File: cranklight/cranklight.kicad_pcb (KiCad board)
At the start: 2 copper layers, 80 x 35 mm, 24 parts, among them J1 Battery, J2 Bulb socket, Q1 Q_NMOS_GDS, SW1 SW_4PDT, U1 WeMos_mini, U2 PTN04050CAD

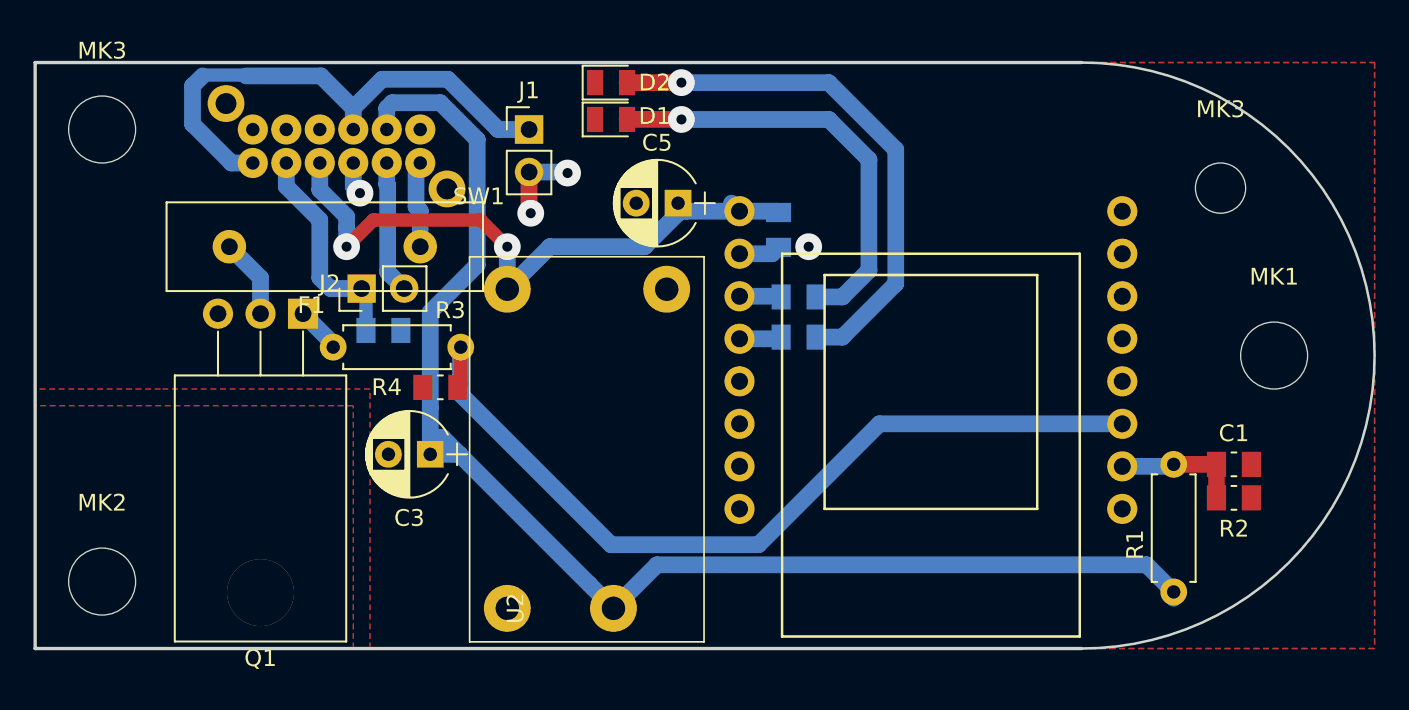
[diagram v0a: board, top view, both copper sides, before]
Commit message: Add fixes: move PTC, add charging connector, use switch as a simple switch
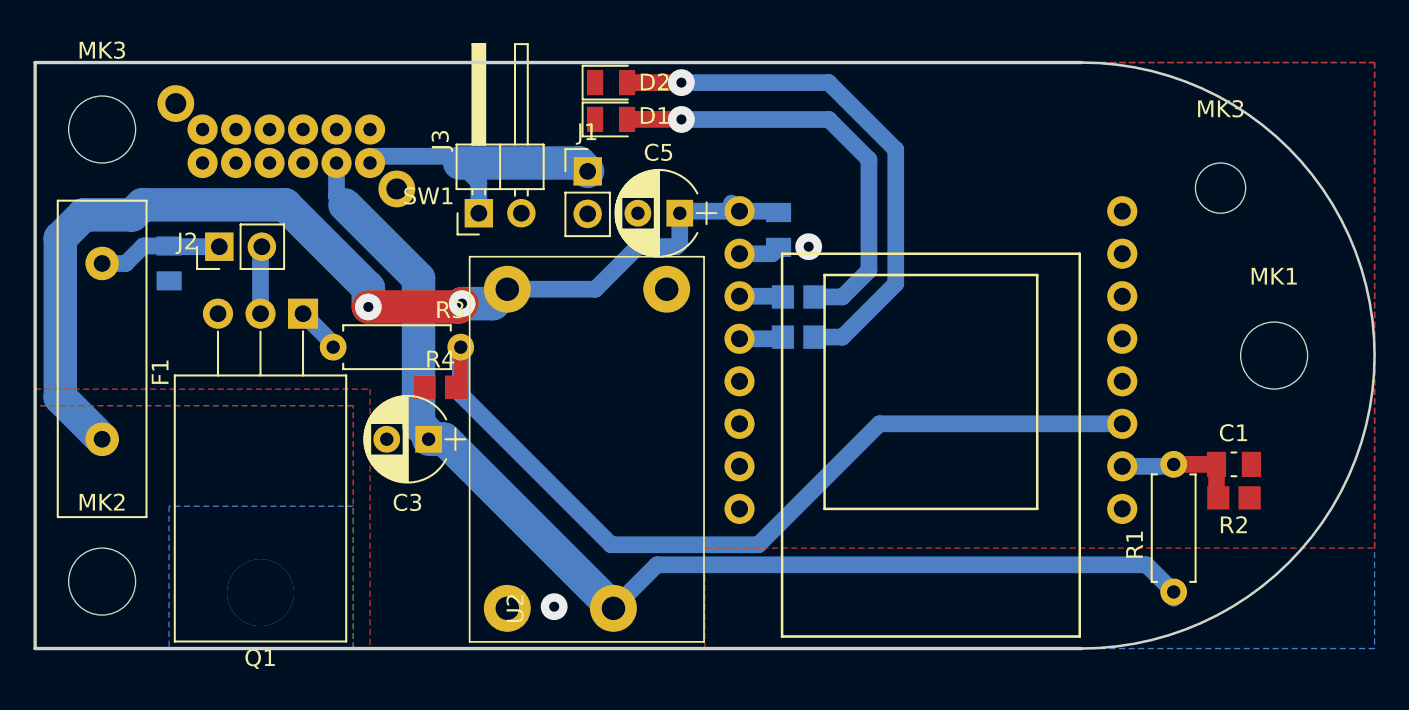
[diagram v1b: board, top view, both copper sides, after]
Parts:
- added J3: Charge, Pin_Headers:Pin_Header_Angled_1x02_Pitch2.54mm, F.Cu at (126.5, 109.0)
- R2, R5, R6: footprint Resistors_SMD:R_0805_2012Metric_Pad1.15x1.50mm_HandSolder -> Resistors_SMD:R_0805_2012Metric_Pad1.33x1.40mm_HandSolder
- R4: value 1M -> 100k; footprint Resistors_SMD:R_0805_2012Metric_Pad1.15x1.50mm_HandSolder -> Resistors_SMD:R_0805_2012Metric_Pad1.33x1.40mm_HandSolder
- moved F1 19.0 mm to (104.0, 112.0), turned to 270 degrees
- moved C4 13.4 mm to (108.0, 112.0), turned to 270 degrees
- moved J2 8.86 mm to (111.0, 111.0)
- moved J1 4.30 mm to (133.0, 106.5)
- moved SW1 3.00 mm to (120.0, 104.0)
- moved C3 0.91 mm to (123.5, 122.5)
- moved C5 0.61 mm to (138.5, 109.0)
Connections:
- F1 pad 1: Net-(F1-Pad1) -> Net-(C4-Pad1)
- F1 pad 2: Net-(F1-Pad2) -> +5V
- Q1 pad 2: Net-(F1-Pad2) -> Net-(J2-Pad2)
- SW1 pad 1: Net-(SW1-Pad1) -> (no net)
- SW1 pad 10: GND -> Net-(SW1-Pad10)
- SW1 pad 11: Net-(J2-Pad2) -> VCC
- SW1 pad 12: Net-(F1-Pad1) -> +BATT
- SW1 pad 2: VCC -> (no net)
- SW1 pad 3: +BATT -> (no net)
- SW1 pad 7: +BATT -> (no net)
- SW1 pad 8: Net-(C4-Pad1) -> (no net)
- SW1 pad 9: +5V -> (no net)
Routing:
- net +5V: track 38.7 -> 63.7 mm
- net +BATT: track 31.3 -> 17.0 mm
- net VCC: track 80.2 -> 69.4 mm
- net GND: track 9.28 -> 2.49 mm, vias 4 -> 2
- net Net-(C4-Pad1): track 13.1 -> 7.45 mm
- net Net-(F1-Pad2): track 4.77 -> 0.00 mm
- net Net-(F1-Pad1): track 4.21 -> 0.00 mm
- net Net-(J2-Pad2): track 7.93 -> 4.03 mm
- added copper zone on F.Cu, net Net-(J2-Pad2)
- removed copper zone on F.Cu, net Net-(F1-Pad2)
